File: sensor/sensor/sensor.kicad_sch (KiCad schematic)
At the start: 29 parts, among them J1 RJ12_Shielded, J2 Conn_01x04, J3 Conn_01x06, SW0 SW_SPDT, SW1 SW_SPDT, SW2 SW_SPDT, SW3 SW_SPDT, U1 PCA9615DP, U2 LTC4316xDD, U5 TPS73101DBV

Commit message: created slide switch footprint, assigned resistor and switch footprints
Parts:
- R12, R13, R24, R25: footprint (none) -> Resistor_SMD:R_0603_1608Metric_Pad0.98x0.95mm_HandSolder
- SW0, SW1, SW2: footprint (none) -> RJ12_Pin_Connector:Slide_SPDT_AS12AH
- SW3: footprint (none) -> Button_Switch_THT:SW_Slide_SPDT_Straight_CK_OS102011MS2Q
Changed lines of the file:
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@@
 	(wire
 		(pts
-			(xy 100.33 113.03) (xy 105.41 113.03)
-		)
-		(stroke
-			(width 0)
-			(type default)
-		)
-	)
-	(wire
-		(pts
 			(xy 173.99 83.82) (xy 186.69 83.82)
 		)
@@
 			)
 		)
-		(property "Footprint" ""
+		(property "Footprint" "RJ12_Pin_Connector:Slide_SPDT_AS12AH"
 			(at 92.71 138.43 0)
 			(effects
@@
 			)
 		)
-		(property "Footprint" ""
+		(property "Footprint" "Resistor_SMD:R_0603_1608Metric_Pad0.98x0.95mm_HandSolder"
 			(at 83.82 122.428 90)
 			(effects
@@
 			)
 		)
-		(property "Footprint" ""
+		(property "Footprint" "Resistor_SMD:R_0603_1608Metric_Pad0.98x0.95mm_HandSolder"
 			(at 83.82 140.208 90)
 			(effects
@@
 			)
 		)
-		(property "Footprint" ""
+		(property "Footprint" "Button_Switch_THT:SW_Slide_SPDT_Straight_CK_OS102011MS2Q"
 			(at 92.71 120.65 0)
 			(effects
@@
 			)
 		)
-		(property "Footprint" ""
+		(property "Footprint" "Resistor_SMD:R_0603_1608Metric_Pad0.98x0.95mm_HandSolder"
 			(at 83.82 131.318 90)
 			(effects
@@
 			)
 		)
-		(property "Footprint" ""
+		(property "Footprint" "Resistor_SMD:R_0603_1608Metric_Pad0.98x0.95mm_HandSolder"
 			(at 83.82 149.098 90)
 			(effects
@@
 			)
 		)
-		(property "Footprint" ""
+		(property "Footprint" "RJ12_Pin_Connector:Slide_SPDT_AS12AH"
 			(at 92.71 147.32 0)
 			(effects
@@
 	)
 	(symbol
-		(lib_id "power:GND")
-		(at 105.41 113.03 0)
-		(unit 1)
-		(exclude_from_sim no)
-		(in_bom yes)
-		(on_board yes)
-		(dnp no)
-		(fields_autoplaced yes)
-		(property "Reference" "#PWR042"
-			(at 105.41 119.38 0)
-			(effects
-				(font
-					(size 1.27 1.27)
-				)
-				(hide yes)
-			)
-		)
-		(property "Value" "GND"
-			(at 105.41 118.11 0)
-			(effects
-				(font
-					(size 1.27 1.27)
-				)
-			)
-		)
-		(property "Footprint" ""
-			(at 105.41 113.03 0)
-			(effects
-				(font
-					(size 1.27 1.27)
-				)
-				(hide yes)
-			)
-		)
-		(property "Datasheet" ""
-			(at 105.41 113.03 0)
-			(effects
-				(font
-					(size 1.27 1.27)
-				)
-				(hide yes)
-			)
-		)
-		(property "Description" "Power symbol creates a global label with name \"GND\" , ground"
-			(at 105.41 113.03 0)
-			(effects
-				(font
-					(size 1.27 1.27)
-				)
-				(hide yes)
-			)
-		)
-		(pin "1"
-		)
-		(instances
-			(project ""
-				(path "/46f6a130-b02e-4523-867c-7812ad0e1543"
-					(reference "#PWR042")
-					(unit 1)
-				)
-			)
-		)
-	)
-	(symbol
 		(lib_id "power:+5V")
 		(at 25.4 170.18 90)
@@
 			)
 		)
-		(property "Footprint" ""
+		(property "Footprint" "RJ12_Pin_Connector:Slide_SPDT_AS12AH"
 			(at 92.71 129.54 0)
 			(effects

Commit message: update
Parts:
- J2: footprint Connector_JST:JST_SH_SM03B-SRSS-TB_1x03-1MP_P1.00mm_Horizontal -> Connector_JST:JST_SH_SM04B-SRSS-TB_1x04-1MP_P1.00mm_Horizontal
- J3: footprint Connector_JST:JST_SH_SM03B-SRSS-TB_1x03-1MP_P1.00mm_Horizontal -> Connector_JST:JST_SH_SM06B-SRSS-TB_1x06-1MP_P1.00mm_Horizontal
- SW0, SW1, SW2: footprint RJ12_Pin_Connector:Slide_SPDT_AS12AH -> (none)
- SW3: footprint Button_Switch_THT:SW_Slide_SPDT_Straight_CK_OS102011MS2Q -> (none)
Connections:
- net scl renamed Sensors/scl
- net sda renamed Sensors/sda
- no-connect marks 0 -> 2
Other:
- sheet Sensors ports: added scl, sda; removed none
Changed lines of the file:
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@@
 		(color 0 0 0 0)
 	)
+	(no_connect
+		(at 52.07 97.79)
+	)
+	(no_connect
+		(at 223.52 97.79)
+	)
 	(wire
 		(pts
@@
 		)
 	)
-	(hierarchical_label "sda"
-		(shape input)
-		(at 44.45 107.95 180)
-		(effects
-			(font
-				(size 1.27 1.27)
-			)
-			(justify right)
-		)
-	)
-	(hierarchical_label "scl"
-		(shape input)
-		(at 44.45 105.41 180)
-		(effects
-			(font
-				(size 1.27 1.27)
-			)
-			(justify right)
-		)
-	)
 	(symbol
 		(lib_id "Interface_Expansion:LTC4316xDD")
@@
 			)
 		)
-		(property "Footprint" "RJ12_Pin_Connector:Slide_SPDT_AS12AH"
+		(property "Footprint" ""
 			(at 92.71 138.43 0)
 			(effects
@@
 			)
 		)
-		(property "Footprint" "Connector_JST:JST_SH_SM03B-SRSS-TB_1x03-1MP_P1.00mm_Horizontal"
+		(property "Footprint" "Connector_JST:JST_SH_SM06B-SRSS-TB_1x06-1MP_P1.00mm_Horizontal"
 			(at 254 107.95 0)
 			(effects
@@
 			)
 		)
-		(property "Footprint" "Button_Switch_THT:SW_Slide_SPDT_Straight_CK_OS102011MS2Q"
+		(property "Footprint" ""
 			(at 92.71 120.65 0)
 			(effects
@@
 			)
 		)
-		(property "Footprint" "Connector_JST:JST_SH_SM03B-SRSS-TB_1x03-1MP_P1.00mm_Horizontal"
+		(property "Footprint" "Connector_JST:JST_SH_SM04B-SRSS-TB_1x04-1MP_P1.00mm_Horizontal"
 			(at 118.11 127 0)
 			(effects
@@
 			)
 		)
-		(property "Footprint" "RJ12_Pin_Connector:Slide_SPDT_AS12AH"
+		(property "Footprint" ""
 			(at 92.71 147.32 0)
 			(effects
@@
 			)
 		)
-		(property "Footprint" "RJ12_Pin_Connector:Slide_SPDT_AS12AH"
+		(property "Footprint" ""
 			(at 92.71 129.54 0)
 			(effects
@@
 			)
 		)
+		(pin "scl" input
+			(at 44.45 105.41 0)
+			(effects
+				(font
+					(size 1.27 1.27)
+				)
+				(justify right)
+			)
+		)
+		(pin "sda" input
+			(at 44.45 107.95 0)
+			(effects
+				(font
+					(size 1.27 1.27)
+				)
+				(justify right)
+			)
+		)

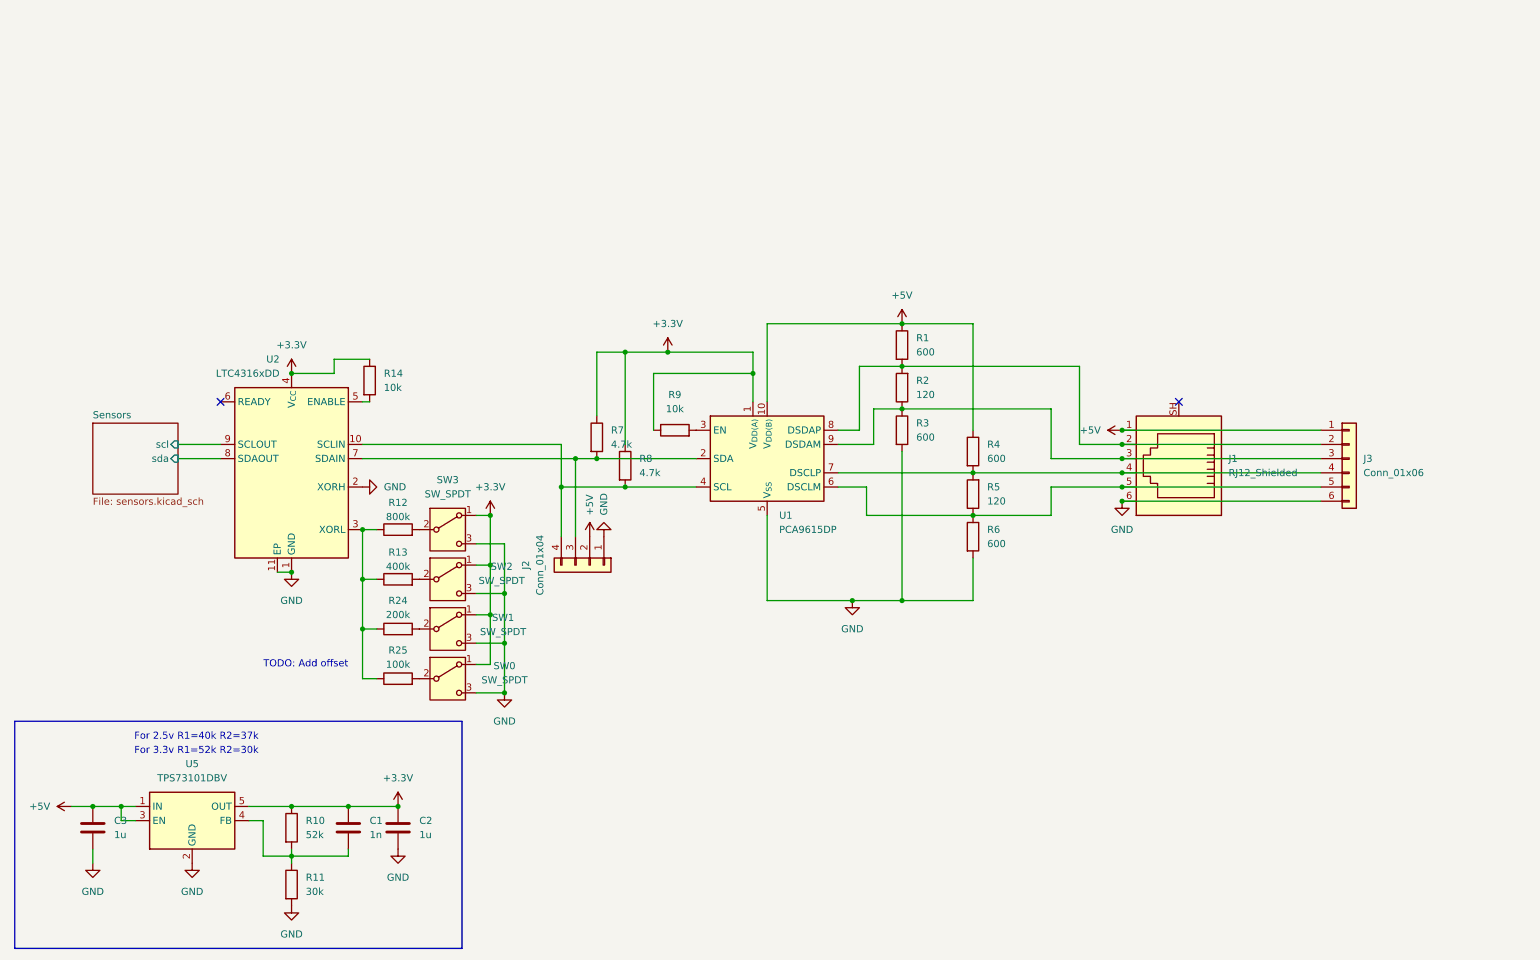
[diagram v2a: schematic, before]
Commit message: updated DAC and started board placement
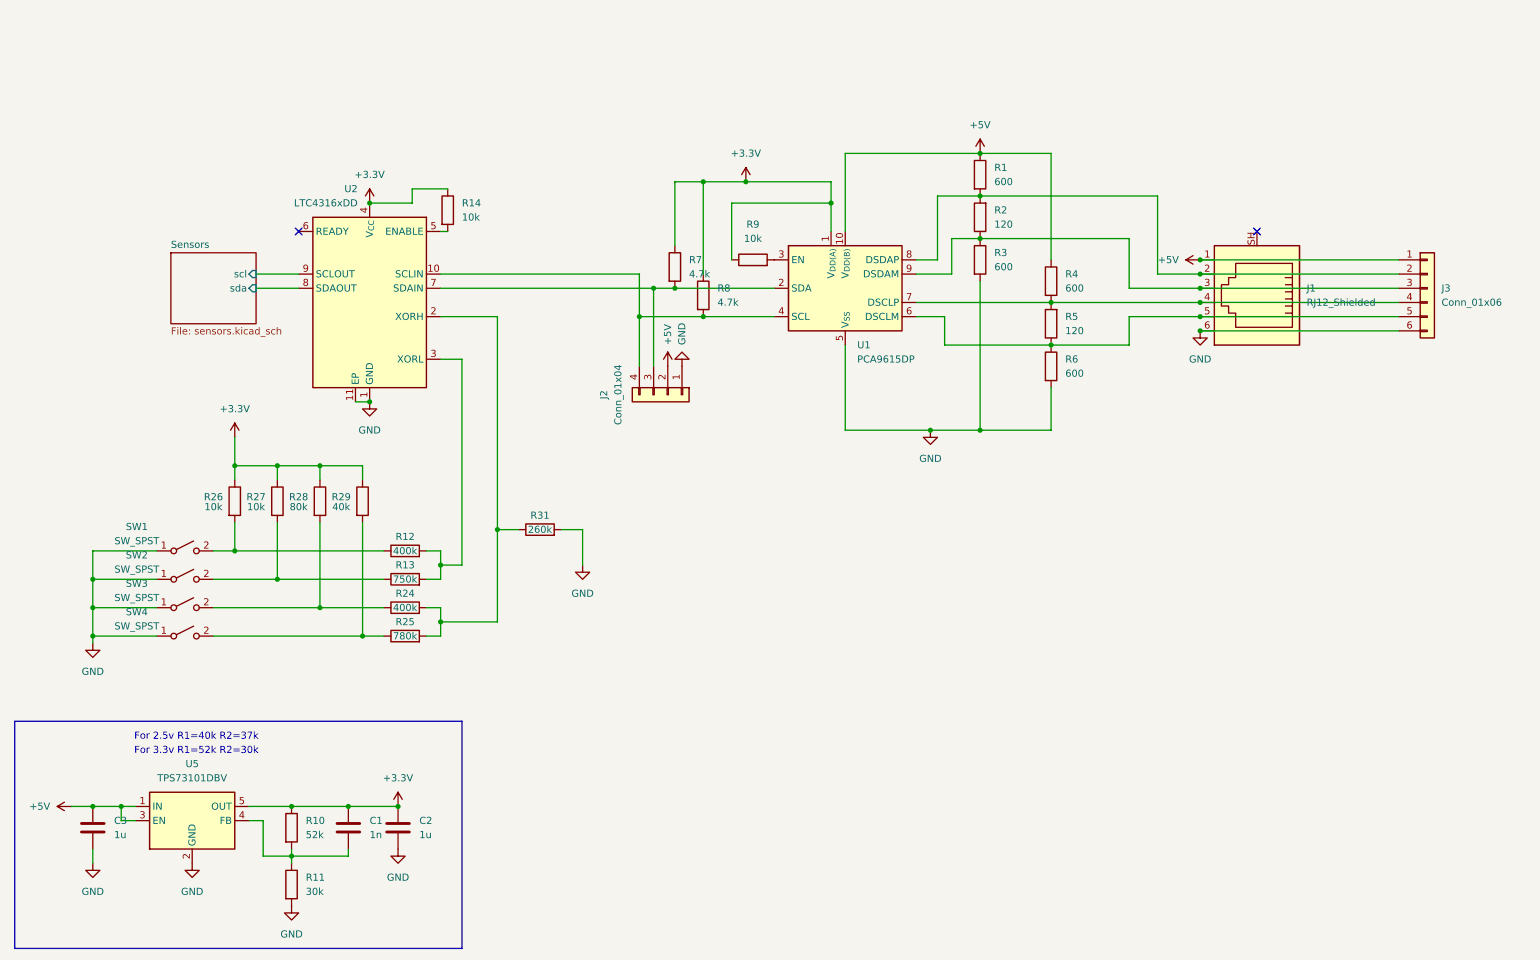
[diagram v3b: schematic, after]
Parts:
- removed SW0, SW1, SW2, SW3: SW_SPDT, symbol Switch:SW_SPDT
- added R26, R27: 10k, Resistor_SMD:R_0603_1608Metric_Pad0.98x0.95mm_HandSolder, symbol Device:R
- added R28: 80k, Resistor_SMD:R_0603_1608Metric_Pad0.98x0.95mm_HandSolder, symbol Device:R
- added R29: 40k, Resistor_SMD:R_0603_1608Metric_Pad0.98x0.95mm_HandSolder, symbol Device:R
- added R31: 260k, Resistor_SMD:R_0603_1608Metric_Pad0.98x0.95mm_HandSolder, symbol Device:R
- added SW1, SW2, SW3, SW4: SW_SPST, symbol Switch:SW_SPST
- R12: value 800k -> 400k
- R13: value 400k -> 750k
- R24: value 200k -> 400k
- R25: value 100k -> 780k
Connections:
- net +3.3V: now also R26.1, R27.1, R28.1, R29.1
- net GND: now also R31.2, SW1.1 (A), SW2.1 (A), SW3.1 (A), SW4.1 (A); no longer U2.2 (XORH)
- net at R24.2: now also R25.2, U2.2 (XORH), R31.1
- net at R12.2: now also R13.2, U2.3 (XORL)
- new net: R13.1, R27.2, SW2.2 (B)
- new net: R12.1, R26.2, SW1.2 (B)
- new net: R25.1, R29.2, SW4.2 (B)
- new net: R24.1, R28.2, SW3.2 (B)
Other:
- note removed: "TODO: Add offset"
- moved on the sheet: J1, J2, J3, R1, R14, R2, R3, R4, R5, R6, R7, R8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

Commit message: half way done with board
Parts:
- removed SW1, SW2, SW3, SW4: SW_SPST, symbol Switch:SW_SPST
- added SW5: SW_Coded_SH-7050, RJ12_Pin_Connector:Rotary_Switch_16_pos, symbol Switch:SW_Coded_SH-7050
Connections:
- net GND: now also SW5.C
- net at R13.1, R27.2: now also SW5.2
- net at R12.1, R26.2: now also SW5.1
- net at R25.1, R29.2: now also SW5.8
- net at R24.1, R28.2: now also SW5.4

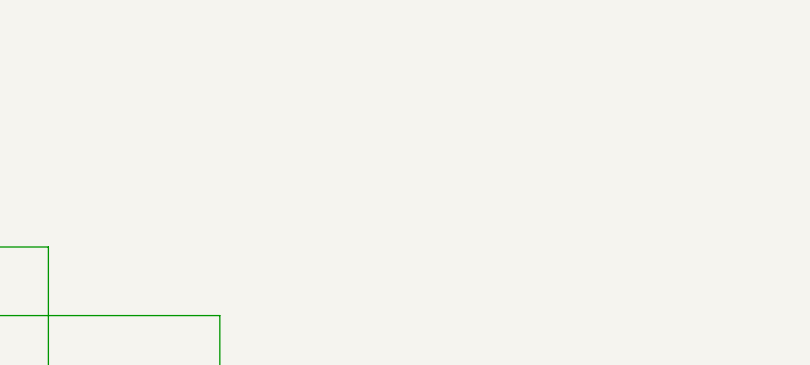
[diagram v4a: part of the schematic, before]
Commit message: began wiring PCB
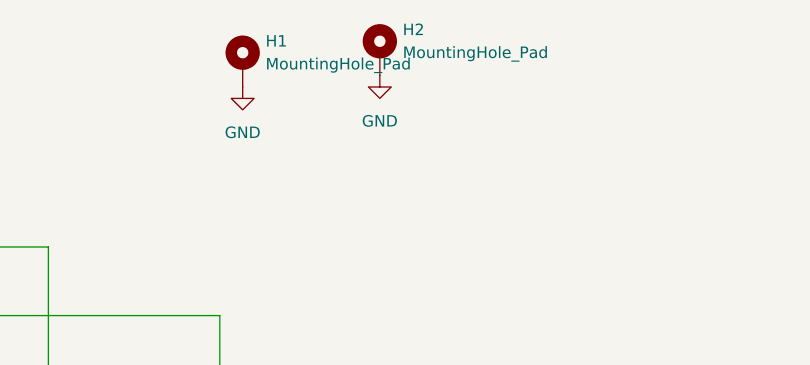
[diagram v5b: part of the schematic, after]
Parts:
- added H1, H2: MountingHole_Pad, MountingHole:MountingHole_4.5mm_Pad_TopOnly, symbol Mechanical:MountingHole_Pad
- C1: footprint Capacitor_SMD:C_0603_1608Metric_Pad1.08x0.95mm_HandSolder -> Capacitor_SMD:C_0402_1005Metric_Pad0.74x0.62mm_HandSolder
- R1, R10, R11, R12, R13, R14, R2, R24, R25, R26, R27, R28, R29, R3, R31, R4, R5, R6, R7, R8, R9: footprint Resistor_SMD:R_0603_1608Metric_Pad0.98x0.95mm_HandSolder -> Resistor_SMD:R_0402_1005Metric_Pad0.72x0.64mm_HandSolder
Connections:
- net GND: now also H1.1, H2.1

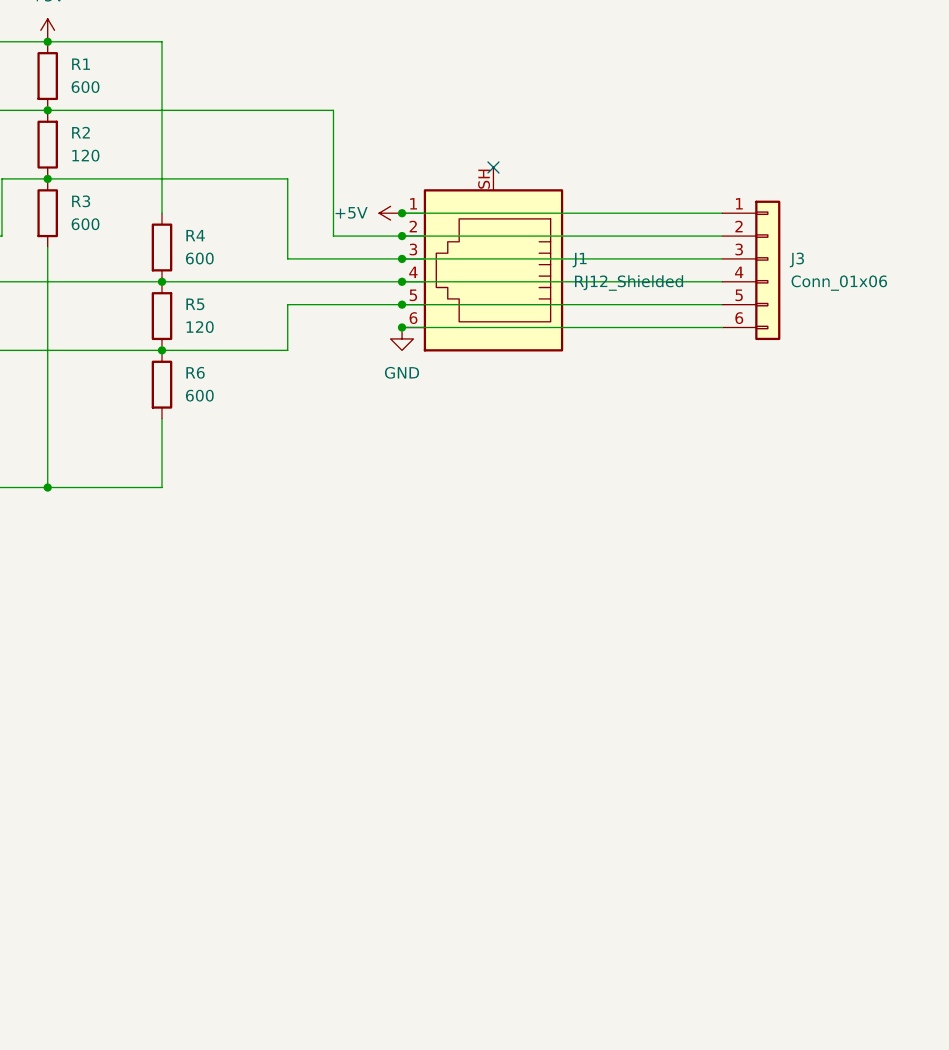
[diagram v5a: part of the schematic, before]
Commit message: new proximity sensor schematic + output RJ12 connectore (pls double check this im just assuming they connect in series)
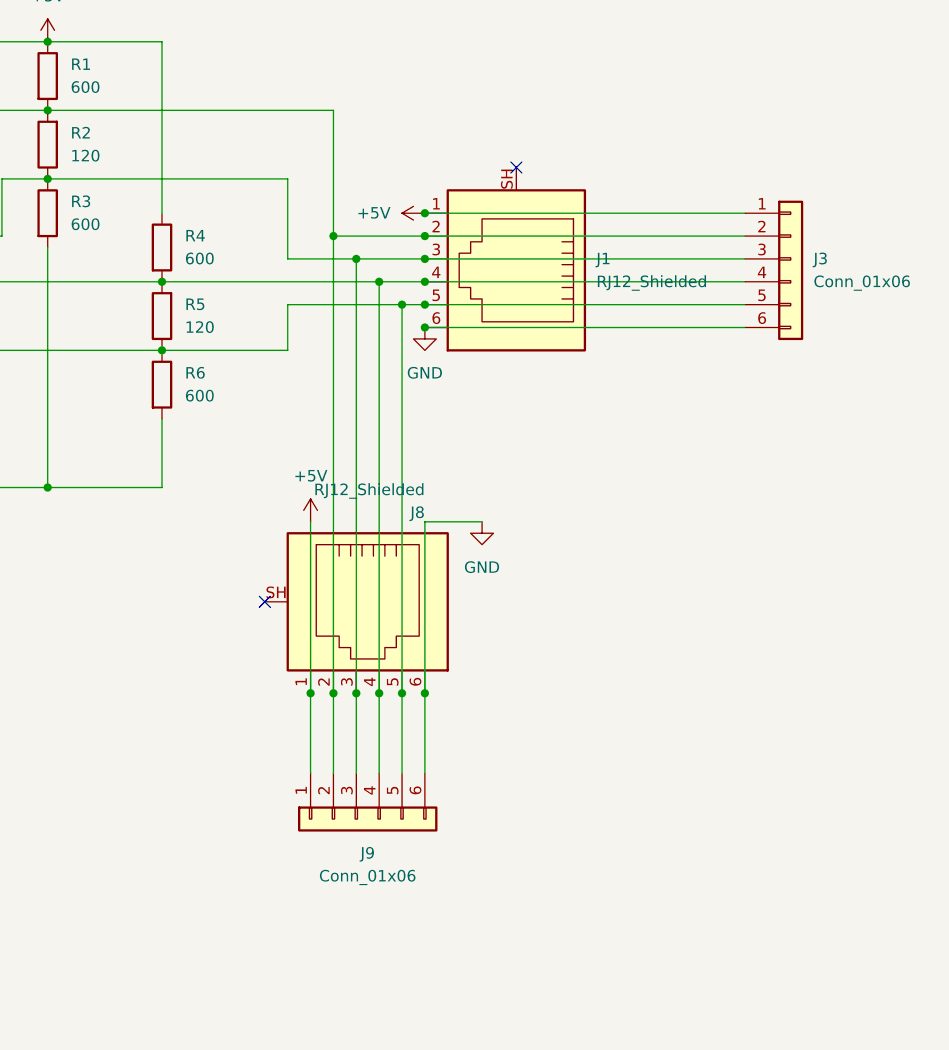
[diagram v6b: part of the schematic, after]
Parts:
- added J8: RJ12_Shielded, RJ12_Pin_Connector:RJ12_Pin_Connector, symbol Connector:RJ12_Shielded
- added J9: Conn_01x06, Connector_JST:JST_SH_SM06B-SRSS-TB_1x06-1MP_P1.00mm_Horizontal, symbol Connector_Generic:Conn_01x06
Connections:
- net +5V: now also J8.1, J9.1 (Pin_1)
- net GND: now also J8.6, J9.6 (Pin_6)
- net at J1.2, J3.2 (Pin_2), R1.2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: now also J8.2, J9.2 (Pin_2)
- net at J1.3, J3.3 (Pin_3), R2.1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: now also J8.3, J9.3 (Pin_3)
- net at J1.4, J3.4 (Pin_4), R4.2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: now also J8.4, J9.4 (Pin_4)
- net at J1.5, J3.5 (Pin_5), R5.1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: now also J8.5, J9.5 (Pin_5)
- no-connect marks 2 -> 3
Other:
- moved on the sheet: J1, J3

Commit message: sensor BOM
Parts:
- C1, C2, C3, R1, R10, R11, R12, R13, R14, R2, R24, R25, R26, R27, R28, R29, R3, R31, R4, R5, R6, R7, R8, R9, U1, U2: Supplier Name (none) -> JLCPCB
- J1, J8, SW5: now left out of the parts list
- J2: Manufacturer_Part_Number (none) -> XY-SM04B-SRSS-TB; Supplier Name (none) -> JLCPCB; Supplier Part Number (none) -> C51940130
- J3, J9: Manufacturer_Part_Number (none) -> SM06B-SRSS-TB(LF)(SN); Supplier Name (none) -> JLCPCB; Supplier Part Number (none) -> C160405
- U5: Manufacturer_Part_Number (none) -> TPS73101DBV; Supplier Name (none) -> JLCPCB
